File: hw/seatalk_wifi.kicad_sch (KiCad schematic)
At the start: 41 parts

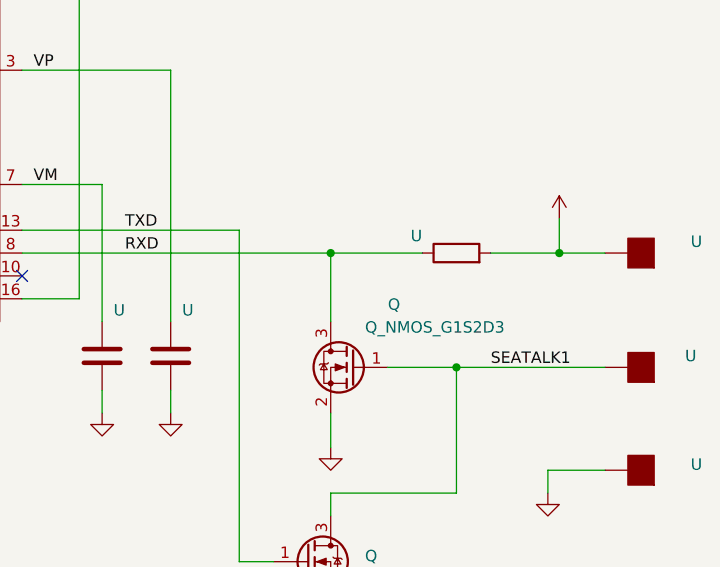
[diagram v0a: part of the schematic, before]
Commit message: Added R12 which allows an RS232 to WiFi bridge function.
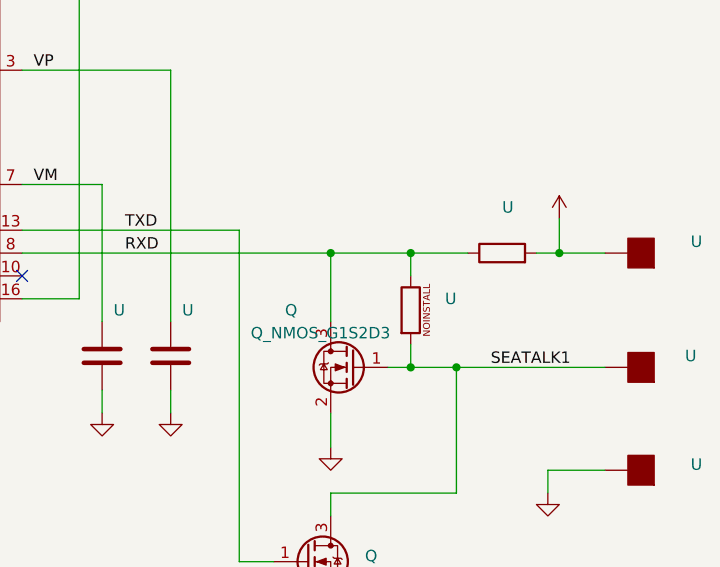
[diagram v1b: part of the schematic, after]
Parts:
- added U: (no value), symbol device:R_NOINSTALL
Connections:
- net RXD: now also U.1
- net SEATALK1: now also U.2
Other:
- moved on the sheet: U
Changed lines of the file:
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@@
   (junction (at 180.34 48.26) (diameter 0) (color 0 0 0 0)
   )
+  (junction (at 238.76 114.3) (diameter 0) (color 0 0 0 0)
+  )
   (junction (at 130.81 162.56) (diameter 0) (color 0 0 0 0)
   )
@@
   )
   (junction (at 120.65 177.8) (diameter 0) (color 0 0 0 0)
+  )
+  (junction (at 238.76 101.6) (diameter 0) (color 0 0 0 0)
   )
   (no_connect (at 58.42 91.44))
@@
     (stroke (width 0) (type default))
   )
-  (wire (pts (xy 247.65 101.6) (xy 255.27 101.6))
+  (wire (pts (xy 252.73 101.6) (xy 255.27 101.6))
     (stroke (width 0) (type default))
   )
@@
     (stroke (width 0) (type default))
   )
-  (wire (pts (xy 229.87 101.6) (xy 240.03 101.6))
+  (wire (pts (xy 229.87 101.6) (xy 238.76 101.6))
     (stroke (width 0) (type default))
   )
@@
     (stroke (width 0) (type default))
   )
+  (wire (pts (xy 238.76 101.6) (xy 245.11 101.6))
+    (stroke (width 0) (type default))
+  )
   (wire (pts (xy 45.72 83.82) (xy 38.1 83.82))
     (stroke (width 0) (type default))
@@
   )
   (wire (pts (xy 109.22 104.14) (xy 109.22 107.95))
+    (stroke (width 0) (type default))
+  )
+  (wire (pts (xy 238.76 111.76) (xy 238.76 114.3))
     (stroke (width 0) (type default))
   )
@@
     (stroke (width 0) (type default))
   )
+  (wire (pts (xy 238.76 114.3) (xy 243.84 114.3))
+    (stroke (width 0) (type default))
+  )
   (wire (pts (xy 127 78.74) (xy 127 101.6))
     (stroke (width 0) (type default))
@@
     (stroke (width 0) (type default))
   )
+  (wire (pts (xy 238.76 101.6) (xy 238.76 104.14))
+    (stroke (width 0) (type default))
+  )
   (wire (pts (xy 96.52 167.64) (xy 109.22 167.64))
     (stroke (width 0) (type default))
@@
     (stroke (width 0) (type default))
   )
-  (wire (pts (xy 236.22 114.3) (xy 243.84 114.3))
+  (wire (pts (xy 236.22 114.3) (xy 238.76 114.3))
     (stroke (width 0) (type default))
   )
@@
     (pin "1")
   )
-  (symbol (lib_id "device:R") (at 243.84 101.6 90) (unit 1)
-    (in_bom yes) (on_board yes)
-    (default_instance (reference "U") (unit 1) (value "") (footprint ""))
-    (property "Reference" "U" (id 0) (at 240.03 99.695 90)
-      (effects (font (size 1.27 1.27)) (justify left))
-    )
-    (property "Value" "" (id 1) (at 252.095 99.695 90)
-      (effects (font (size 1.27 1.27)) (justify left))
-    )
-    (property "Footprint" "" (id 2) (at 243.84 103.378 90)
-      (effects (font (size 1.27 1.27)) hide)
-    )
-    (property "Datasheet" "~" (id 3) (at 255.27 101.6 0)
-      (effects (font (size 1.27 1.27)) hide)
-    )
-    (property "MFG" "N/A" (id 4) (at 250.19 101.6 0)
-      (effects (font (size 1.27 1.27)) hide)
-    )
-    (property "MPN" "N/A" (id 5) (at 252.73 101.6 0)
-      (effects (font (size 1.27 1.27)) hide)
-    )
-    (property "Digikey PN" "N/A" (id 6) (at 257.81 101.6 0)
-      (effects (font (size 1.27 1.27)) hide)
-    )
-    (property "Mouser PN" "N/A" (id 7) (at 260.35 101.6 0)
-      (effects (font (size 1.27 1.27)) hide)
-    )
-    (property "Power" "N/A" (id 8) (at 262.89 101.6 0)
-      (effects (font (size 1.27 1.27)) hide)
-    )
-    (property "Tolerance" "N/A" (id 9) (at 262.89 101.6 0)
-      (effects (font (size 1.27 1.27)) hide)
-    )
-    (property "Datasheet_1" "N/A" (id 10) (at 255.27 101.6 0)
+  (symbol (lib_id "device:R") (at 248.92 101.6 90) (unit 1)
+    (in_bom yes) (on_board yes)
+    (default_instance (reference "U") (unit 1) (value "") (footprint ""))
+    (property "Reference" "U" (id 0) (at 250.19 96.52 90)
+      (effects (font (size 1.27 1.27)) (justify left))
+    )
+    (property "Value" "" (id 1) (at 251.46 99.06 90)
+      (effects (font (size 1.27 1.27)) (justify left))
+    )
+    (property "Footprint" "" (id 2) (at 248.92 103.378 90)
+      (effects (font (size 1.27 1.27)) hide)
+    )
+    (property "Datasheet" "~" (id 3) (at 260.35 101.6 0)
+      (effects (font (size 1.27 1.27)) hide)
+    )
+    (property "MFG" "N/A" (id 4) (at 255.27 101.6 0)
+      (effects (font (size 1.27 1.27)) hide)
+    )
+    (property "MPN" "N/A" (id 5) (at 257.81 101.6 0)
+      (effects (font (size 1.27 1.27)) hide)
+    )
+    (property "Digikey PN" "N/A" (id 6) (at 262.89 101.6 0)
+      (effects (font (size 1.27 1.27)) hide)
+    )
+    (property "Mouser PN" "N/A" (id 7) (at 265.43 101.6 0)
+      (effects (font (size 1.27 1.27)) hide)
+    )
+    (property "Power" "N/A" (id 8) (at 267.97 101.6 0)
+      (effects (font (size 1.27 1.27)) hide)
+    )
+    (property "Tolerance" "N/A" (id 9) (at 267.97 101.6 0)
+      (effects (font (size 1.27 1.27)) hide)
+    )
+    (property "Datasheet_1" "N/A" (id 10) (at 260.35 101.6 0)
       (effects (font (size 1.27 1.27)) hide)
     )
@@
     (in_bom yes) (on_board yes)
     (default_instance (reference "Q") (unit 1) (value "Q_NMOS_G1S2D3") (footprint ""))
-    (property "Reference" "Q" (id 0) (at 236.22 107.315 0)
+    (property "Reference" "Q" (id 0) (at 224.79 107.95 0)
       (effects (font (size 1.27 1.27)) (justify right))
     )
-    (property "Value" "Q_NMOS_G1S2D3" (id 1) (at 233.68 109.855 0)
+    (property "Value" "Q_NMOS_G1S2D3" (id 1) (at 220.98 110.49 0)
       (effects (font (size 1.27 1.27)) (justify right))
     )
@@
     )
     (pin "1")
+  )
+  (symbol (lib_id "device:R_NOINSTALL") (at 238.76 107.95 0) (unit 1)
+    (in_bom yes) (on_board yes)
+    (default_instance (reference "U") (unit 1) (value "") (footprint ""))
+    (property "Reference" "U" (id 0) (at 242.57 106.68 0)
+      (effects (font (size 1.27 1.27)) (justify left))
+    )
+    (property "Value" "" (id 1) (at 242.57 109.22 0)
+      (effects (font (size 1.27 1.27)) (justify left))
+    )
+    (property "Footprint" "" (id 2) (at 236.982 107.95 90)
+      (effects (font (size 1.27 1.27)) hide)
+    )
+    (property "Datasheet" "~" (id 3) (at 238.76 107.95 0)
+      (effects (font (size 1.27 1.27)) hide)
+    )
+    (property "MFG" "N/A" (id 4) (at 238.76 114.3 0)
+      (effects (font (size 1.27 1.27)) hide)
+    )
+    (property "MPN" "N/A" (id 5) (at 238.76 116.84 0)
+      (effects (font (size 1.27 1.27)) hide)
+    )
+    (property "Digikey PN" "N/A" (id 6) (at 238.76 121.92 0)
+      (effects (font (size 1.27 1.27)) hide)
+    )
+    (property "Mouser PN" "N/A" (id 7) (at 238.76 124.46 0)
+      (effects (font (size 1.27 1.27)) hide)
+    )
+    (property "Power" "N/A" (id 8) (at 238.76 127 0)
+      (effects (font (size 1.27 1.27)) hide)
+    )
+    (property "Tolerance" "N/A" (id 9) (at 238.76 127 0)
+      (effects (font (size 1.27 1.27)) hide)
+    )
+    (property "Datasheet_1" "N/A" (id 10) (at 238.76 119.38 0)
+      (effects (font (size 1.27 1.27)) hide)
+    )
+    (pin "1")
+    (pin "2")
   )
   (symbol (lib_id "power:PWR_FLAG") (at 59.69 161.29 0) (unit 1)
@@
       (reference "R11") (unit 1) (value "1K") (footprint "resistor_SMD:R_0603_1608Metric")
     )
+    (path "/ee3fa035-ea51-4f38-9299-60a64e58e413"
+      (reference "R12") (unit 1) (value "0") (footprint "resistor_SMD:R_0603_1608Metric")
+    )
     (path "/1a9717d8-f4f7-43ef-b00c-6833bbf80e1b"
